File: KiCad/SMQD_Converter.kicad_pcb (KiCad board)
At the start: 2 copper layers, 14.9 x 10.9 mm, 3 parts, among them J1 XTAL, J2 GND, Y1 Crystal_GND24

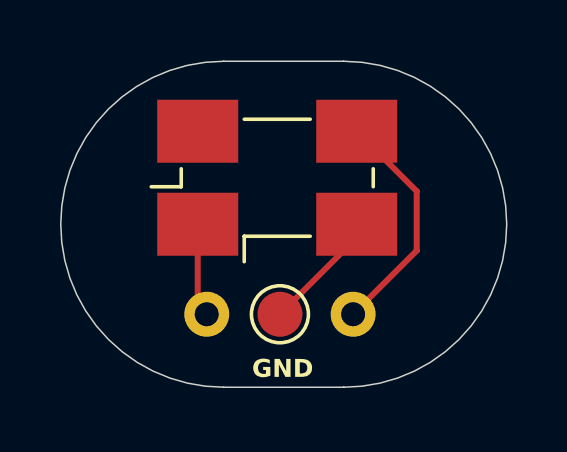
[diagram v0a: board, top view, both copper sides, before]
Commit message: Sent for test fabrication
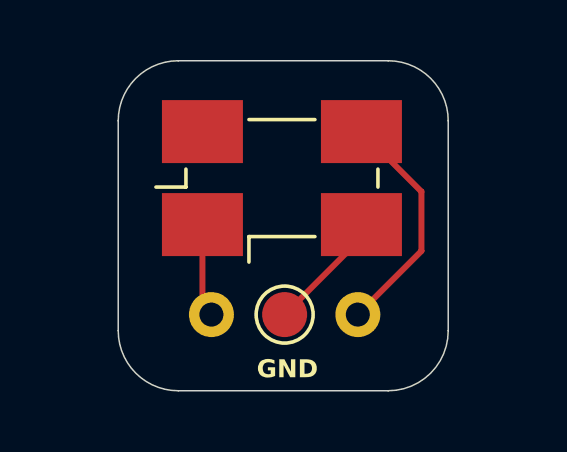
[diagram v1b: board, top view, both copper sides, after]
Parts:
- moved J1 0.16 mm to (83.4, 64.9)
- moved J2 0.16 mm to (85.9, 64.9)
- moved Y1 0.16 mm to (85.8, 60.3)
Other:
- board size 14.9 x 10.9 mm -> 11 x 11 mm
- board text added: "SMQD Crystal Converter Brett Hallen May 2025"
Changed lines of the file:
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@@
 		(allow_soldermask_bridges_in_footprints no)
 		(tenting front back)
-		(grid_origin 127 71.567115)
+		(grid_origin 81.33 57.397115)
 		(pcbplotparams
 			(layerselection 0x00000000_00000000_55555555_5755f5ff)
@@
 	(footprint "Crystal:Crystal_SMD_0603-4Pin_6.0x3.5mm_HandSoldering"
 		(layer "F.Cu")
-		(at 85.63 60.297115)
+		(at 85.787145 60.308348)
 		(descr "SMD Crystal SERIES SMD0603/4 http://www.petermann-technik.de/fileadmin/petermann/pdf/SMD0603-4.pdf, hand-soldering, 6.0x3.5mm^2 package")
 		(tags "SMD SMT crystal hand-soldering")
@@
 	(footprint "Crystal:Crystal_HC49-U_Vertical"
 		(layer "F.Cu")
-		(at 83.28 64.847115)
+		(at 83.437145 64.858348)
 		(descr "Crystal THT HC-49/U http://5hertz.com/pdfs/04404_D.pdf")
 		(tags "THT crystalHC-49/U")
@@
 	(footprint "TestPoint:TestPoint_Pad_D1.5mm"
 		(layer "F.Cu")
-		(at 85.72 64.847115)
+		(at 85.877145 64.858348)
 		(descr "SMD pad as test Point, diameter 1.5mm")
 		(tags "test point SMD pad")
@@
 		(embedded_fonts no)
 	)
-	(gr_line
-		(start 87.85559 67.279993)
-		(end 83.847115 67.28)
+	(gr_arc
+		(start 89.33 56.397115)
+		(mid 90.744214 56.982901)
+		(end 91.33 58.397115)
 		(stroke
 			(width 0.05)
@@
 	)
 	(gr_arc
-		(start 83.847115 67.28)
-		(mid 78.41423 61.847115)
-		(end 83.847115 56.41423)
+		(start 80.33 58.397115)
+		(mid 80.915781 56.982892)
+		(end 82.33 56.397115)
 		(stroke
 			(width 0.05)
@@
 		(layer "Edge.Cuts")
 	)
-	(gr_arc
-		(start 87.847115 56.41423)
-		(mid 93.28 61.847115)
-		(end 87.847115 67.28)
+	(gr_line
+		(start 89.33 67.397115)
+		(end 82.33 67.397115)
 		(stroke
 			(width 0.05)
@@
 	)
 	(gr_line
-		(start 83.847115 56.41423)
-		(end 87.847115 56.41423)
+		(start 91.33 58.397115)
+		(end 91.33 65.397115)
 		(stroke
 			(width 0.05)
@@
 		(layer "Edge.Cuts")
 	)
+	(gr_arc
+		(start 82.33 67.397115)
+		(mid 80.915786 66.811329)
+		(end 80.33 65.397115)
+		(stroke
+			(width 0.05)
+			(type default)
+		)
+		(layer "Edge.Cuts")
+	)
+	(gr_line
+		(start 80.33 65.397115)
+		(end 80.33 58.397115)
+		(stroke
+			(width 0.05)
+			(type default)
+		)
+		(layer "Edge.Cuts")
+	)
+	(gr_arc
+		(start 91.33 65.397115)
+		(mid 90.744208 66.811319)
+		(end 89.33 67.397115)
+		(stroke
+			(width 0.05)
+			(type default)
+		)
+		(layer "Edge.Cuts")
+	)
+	(gr_line
+		(start 82.33 56.397115)
+		(end 89.33 56.397115)
+		(stroke
+			(width 0.05)
+			(type default)
+		)
+		(layer "Edge.Cuts")
+	)
 	(gr_text "GND"
-		(at 84.787974 67.009067 0)
+		(at 84.945119 67.0203 0)
 		(layer "F.SilkS")
 		(effects
@@
 		)
 	)
+	(gr_text "SMQD Crystal\nConverter\nBrett Hallen\nMay 2025"
+		(at 88.33 62.397115 0)
+		(layer "B.SilkS")
+		(effects
+			(font
+				(size 0.5 0.5)
+				(thickness 0.1)
+				(bold yes)
+			)
+			(justify left bottom mirror)
+		)
+	)
 	(segment
-		(start 82.98 61.847115)
-		(end 82.98 64.547115)
+		(start 83.137145 61.858348)
+		(end 83.137145 64.558348)
 		(width 0.2)
 		(layer "F.Cu")
@@
 	)
 	(segment
-		(start 88.28 58.747115)
-		(end 90.28 60.747115)
+		(start 88.437145 58.758348)
+		(end 90.437145 60.758348)
 		(width 0.2)
 		(layer "F.Cu")
@@
 	)
 	(segment
-		(start 90.28 62.727115)
-		(end 88.16 64.847115)
+		(start 90.437145 62.738348)
+		(end 88.317145 64.858348)
 		(width 0.2)
 		(layer "F.Cu")
@@
 	)
 	(segment
-		(start 90.28 60.747115)
-		(end 90.28 62.727115)
+		(start 90.437145 60.758348)
+		(end 90.437145 62.738348)
 		(width 0.2)
 		(layer "F.Cu")
@@
 	)
 	(segment
-		(start 88.28 62.287115)
-		(end 85.72 64.847115)
+		(start 88.437145 62.298348)
+		(end 85.877145 64.858348)
 		(width 0.2)
 		(layer "F.Cu")
@@
 		(net 3)
 	)
-	(group ""
-		(members "26ce57ac-f25e-4705-a297-e7418fcd3671" "38b44ecf-2f04-4ced-bede-e7a4ea4ab63d"
-			"9473b967-8537-4ab4-a417-3ef748d5855d" "aad9ab17-24e5-456f-a68e-35b06bf8645f"
-		)
-	)
 	(embedded_fonts no)
